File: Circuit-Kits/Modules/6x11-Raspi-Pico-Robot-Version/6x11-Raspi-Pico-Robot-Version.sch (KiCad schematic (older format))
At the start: 9 parts, among them J1 PWM, J2 PWM, J3 PWM, J4 PWM, J5 ANALOG, J6 ANALOG, J7 ANALOG, U1 ARDUINO-SERVO-PWM, U2 Pico

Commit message: Updated PCB with new footprint and pinout
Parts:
- removed U1: ARDUINO-SERVO-PWM, Crazy_Circuits:5x11-SERVO-ANALOG, symbol 5x11-Raspi-Pico-Robot-Version-rescue:ARDUINO-SERVO-PWM
- added U1: 6x11-PICO, Crazy_Circuits:6x11-PICO-ROBOT, symbol crazy_circuits:6x11-PICO
- J1, J2, J3, J4, J5, J6, J7: symbol 5x11-Raspi-Pico-Robot-Version-rescue:HEADER-MALE-3POS-TH-1x03-P0.1IN-crazy_circuits -> 6x11-Raspi-Pico-Robot-Version-rescue:HEADER-MALE-3POS-TH-1x03-P0.1IN-crazy_circuits-5x11-Raspi-Pico-Robot-Version-rescue
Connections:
- wire segments 74 -> 75
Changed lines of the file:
@@
 $EndDescr
 $Comp
-L 5x11-Raspi-Pico-Robot-Version-rescue:GND-crazy_circuits #PWR01
+L 6x11-Raspi-Pico-Robot-Version-rescue:GND-crazy_circuits-5x11-Raspi-Pico-Robot-Version-rescue #PWR01
 U 1 1 58FE4F4A
 P 3725 4225
@@
 A5
 $Comp
-L 5x11-Raspi-Pico-Robot-Version-rescue:HEADER-MALE-3POS-TH-1x03-P0.1IN-crazy_circuits J1
+L 6x11-Raspi-Pico-Robot-Version-rescue:HEADER-MALE-3POS-TH-1x03-P0.1IN-crazy_circuits-5x11-Raspi-Pico-Robot-Version-rescue J1
 U 1 1 58FE51EC
 P 3350 1675
@@
 $EndComp
 $Comp
-L 5x11-Raspi-Pico-Robot-Version-rescue:HEADER-MALE-3POS-TH-1x03-P0.1IN-crazy_circuits J5
+L 6x11-Raspi-Pico-Robot-Version-rescue:HEADER-MALE-3POS-TH-1x03-P0.1IN-crazy_circuits-5x11-Raspi-Pico-Robot-Version-rescue J5
 U 1 1 58FE54AA
 P 3350 3575
@@
 $EndComp
 $Comp
-L 5x11-Raspi-Pico-Robot-Version-rescue:HEADER-MALE-3POS-TH-1x03-P0.1IN-crazy_circuits J6
+L 6x11-Raspi-Pico-Robot-Version-rescue:HEADER-MALE-3POS-TH-1x03-P0.1IN-crazy_circuits-5x11-Raspi-Pico-Robot-Version-rescue J6
 U 1 1 58FE54F2
 P 3350 4050
@@
 $EndComp
 $Comp
-L 5x11-Raspi-Pico-Robot-Version-rescue:GND-crazy_circuits #PWR03
+L 6x11-Raspi-Pico-Robot-Version-rescue:GND-crazy_circuits-5x11-Raspi-Pico-Robot-Version-rescue #PWR03
 U 1 1 58FE5E9A
 P 5325 4275
@@
 Connection ~ 3725 3200
 $Comp
-L 5x11-Raspi-Pico-Robot-Version-rescue:HEADER-MALE-3POS-TH-1x03-P0.1IN-crazy_circuits J2
+L 6x11-Raspi-Pico-Robot-Version-rescue:HEADER-MALE-3POS-TH-1x03-P0.1IN-crazy_circuits-5x11-Raspi-Pico-Robot-Version-rescue J2
 U 1 1 5AF1C185
 P 3350 2150
@@
 $EndComp
 $Comp
-L 5x11-Raspi-Pico-Robot-Version-rescue:HEADER-MALE-3POS-TH-1x03-P0.1IN-crazy_circuits J3
+L 6x11-Raspi-Pico-Robot-Version-rescue:HEADER-MALE-3POS-TH-1x03-P0.1IN-crazy_circuits-5x11-Raspi-Pico-Robot-Version-rescue J3
 U 1 1 5AF1C1CE
 P 3350 2625
@@
 $EndComp
 $Comp
-L 5x11-Raspi-Pico-Robot-Version-rescue:HEADER-MALE-3POS-TH-1x03-P0.1IN-crazy_circuits J4
+L 6x11-Raspi-Pico-Robot-Version-rescue:HEADER-MALE-3POS-TH-1x03-P0.1IN-crazy_circuits-5x11-Raspi-Pico-Robot-Version-rescue J4
 U 1 1 5AF1C230
 P 3350 3100
@@
 $EndComp
 $Comp
-L 5x11-Raspi-Pico-Robot-Version-rescue:GND-crazy_circuits #PWR0102
+L 6x11-Raspi-Pico-Robot-Version-rescue:GND-crazy_circuits-5x11-Raspi-Pico-Robot-Version-rescue #PWR0102
 U 1 1 608B12B6
 P 9100 1850
@@
 	9100 1850 8825 1850
 $Comp
-L 5x11-Raspi-Pico-Robot-Version-rescue:GND-crazy_circuits #PWR0103
+L 6x11-Raspi-Pico-Robot-Version-rescue:GND-crazy_circuits-5x11-Raspi-Pico-Robot-Version-rescue #PWR0103
 U 1 1 608BAEE6
 P 9100 2350
@@
 	9100 2350 8825 2350
 $Comp
-L 5x11-Raspi-Pico-Robot-Version-rescue:GND-crazy_circuits #PWR0104
+L 6x11-Raspi-Pico-Robot-Version-rescue:GND-crazy_circuits-5x11-Raspi-Pico-Robot-Version-rescue #PWR0104
 U 1 1 608BCF87
 P 9100 2850
@@
 	9100 2850 8825 2850
 $Comp
-L 5x11-Raspi-Pico-Robot-Version-rescue:GND-crazy_circuits #PWR0105
+L 6x11-Raspi-Pico-Robot-Version-rescue:GND-crazy_circuits-5x11-Raspi-Pico-Robot-Version-rescue #PWR0105
 U 1 1 608BEE78
 P 9100 3350
@@
 	9100 3350 8825 3350
 $Comp
-L 5x11-Raspi-Pico-Robot-Version-rescue:GND-crazy_circuits #PWR0106
+L 6x11-Raspi-Pico-Robot-Version-rescue:GND-crazy_circuits-5x11-Raspi-Pico-Robot-Version-rescue #PWR0106
 U 1 1 608C380D
 P 7150 1850
@@
 	7150 1850 7425 1850
 $Comp
-L 5x11-Raspi-Pico-Robot-Version-rescue:GND-crazy_circuits #PWR0107
+L 6x11-Raspi-Pico-Robot-Version-rescue:GND-crazy_circuits-5x11-Raspi-Pico-Robot-Version-rescue #PWR0107
 U 1 1 608C5761
 P 7150 2350
@@
 	7150 2350 7425 2350
 $Comp
-L 5x11-Raspi-Pico-Robot-Version-rescue:GND-crazy_circuits #PWR0108
+L 6x11-Raspi-Pico-Robot-Version-rescue:GND-crazy_circuits-5x11-Raspi-Pico-Robot-Version-rescue #PWR0108
 U 1 1 608C7766
 P 7150 2850
@@
 	7150 2850 7425 2850
 $Comp
-L 5x11-Raspi-Pico-Robot-Version-rescue:GND-crazy_circuits #PWR0109
+L 6x11-Raspi-Pico-Robot-Version-rescue:GND-crazy_circuits-5x11-Raspi-Pico-Robot-Version-rescue #PWR0109
 U 1 1 608C98C7
 P 7150 3350
@@
 Wire Wire Line
 	7150 3350 7425 3350
-$Comp
-L crazy_circuits:3.3V #PWR0110
-U 1 1 608CB6CC
-P 5475 1200
-F 0 "#PWR0110" H 5475 1050 50  0001 C CNN
-F 1 "3.3V" V 5493 1328 50  0000 L CNN
-F 2 "" H 5475 1200 50  0000 C CNN
-F 3 "" H 5475 1200 50  0000 C CNN
-	1    5475 1200
-	0    -1   -1   0
-$EndComp
 $Comp
 L crazy_circuits:3.3V #PWR0111
@@
 Text GLabel 5475 2500 0    50   Input ~ 0
 IO8
-Text GLabel 5475 2600 0    50   Input ~ 0
-IO9
 Text GLabel 5475 2700 0    50   Input ~ 0
 IO10
@@
 	5475 2300 5700 2300
 $Comp
-L 5x11-Raspi-Pico-Robot-Version-rescue:HEADER-MALE-3POS-TH-1x03-P0.1IN-crazy_circuits J7
+L 6x11-Raspi-Pico-Robot-Version-rescue:HEADER-MALE-3POS-TH-1x03-P0.1IN-crazy_circuits-5x11-Raspi-Pico-Robot-Version-rescue J7
 U 1 1 608A960B
 P 3350 4675
@@
 $EndComp
 $Comp
-L 5x11-Raspi-Pico-Robot-Version-rescue:GND-crazy_circuits #PWR0117
+L 6x11-Raspi-Pico-Robot-Version-rescue:GND-crazy_circuits-5x11-Raspi-Pico-Robot-Version-rescue #PWR0117
 U 1 1 608A9E31
 P 3725 4875
@@
 	4325 3650 4325 4575
 $Comp
-L 5x11-Raspi-Pico-Robot-Version-rescue:GND-crazy_circuits #PWR0119
+L 6x11-Raspi-Pico-Robot-Version-rescue:GND-crazy_circuits-5x11-Raspi-Pico-Robot-Version-rescue #PWR0119
 U 1 1 608B6490
 P 5575 1100
@@
 Wire Wire Line
 	3550 4575 4325 4575
-$Comp
-L 5x11-Raspi-Pico-Robot-Version-rescue:ARDUINO-SERVO-PWM U1
-U 1 1 608DB815
-P 6000 2750
-F 0 "U1" H 5822 2971 50  0000 R CNN
-F 1 "ARDUINO-SERVO-PWM" H 5822 2880 50  0000 R CNN
-F 2 "Crazy_Circuits:5x11-SERVO-ANALOG" H 6000 2750 50  0001 C CNN
-F 3 "" H 6000 2750 50  0001 C CNN
-	1    6000 2750
-	-1   0    0    -1
-$EndComp
 Text GLabel 8825 2150 2    50   Input ~ 0
 AREF
 Text GLabel 5700 1300 0    50   Input ~ 0
 AREF
+$Comp
+L crazy_circuits:6x11-PICO U1
+U 1 1 60AB76E0
+P 5950 2900
+F 0 "U1" H 5722 3271 50  0000 R CNN
+F 1 "6x11-PICO" H 5722 3180 50  0000 R CNN
+F 2 "Crazy_Circuits:6x11-PICO-ROBOT" H 5950 2900 50  0001 C CNN
+F 3 "" H 5950 2900 50  0001 C CNN
+	1    5950 2900
+	-1   0    0    -1
+$EndComp
+$Comp
+L crazy_circuits:3.3V #PWR0110
+U 1 1 608CB6CC
+P 5475 1200
+F 0 "#PWR0110" H 5475 1050 50  0001 C CNN
+F 1 "3.3V" V 5493 1328 50  0000 L CNN
+F 2 "" H 5475 1200 50  0000 C CNN
+F 3 "" H 5475 1200 50  0000 C CNN
+	1    5475 1200
+	0    -1   -1   0
+$EndComp
+Text GLabel 5475 2600 0    50   Input ~ 0
+IO9
+Wire Wire Line
+	5475 2600 5700 2600
 $EndSCHEMATC

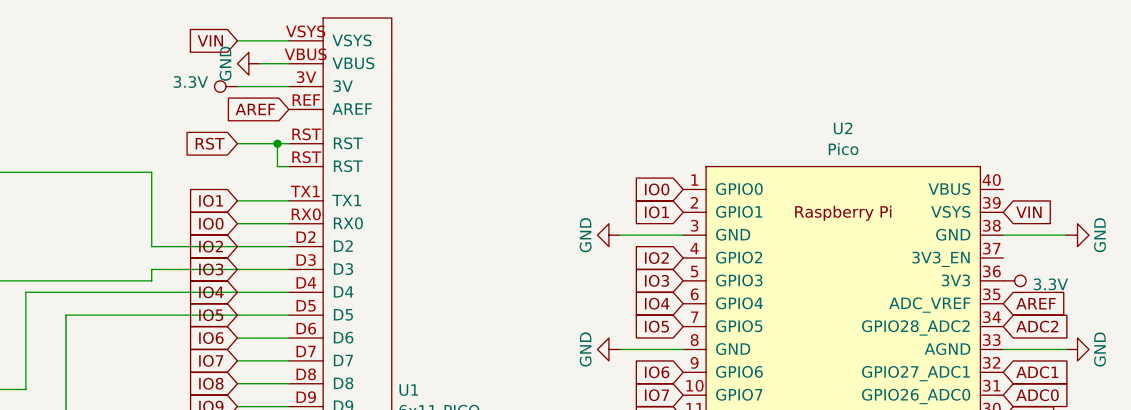
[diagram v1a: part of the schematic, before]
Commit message: Design Changes
* Removed D0 and D16
* Shifted pins
* Added silkscreen labels for 3v
* Broke out VBUS and VSYS
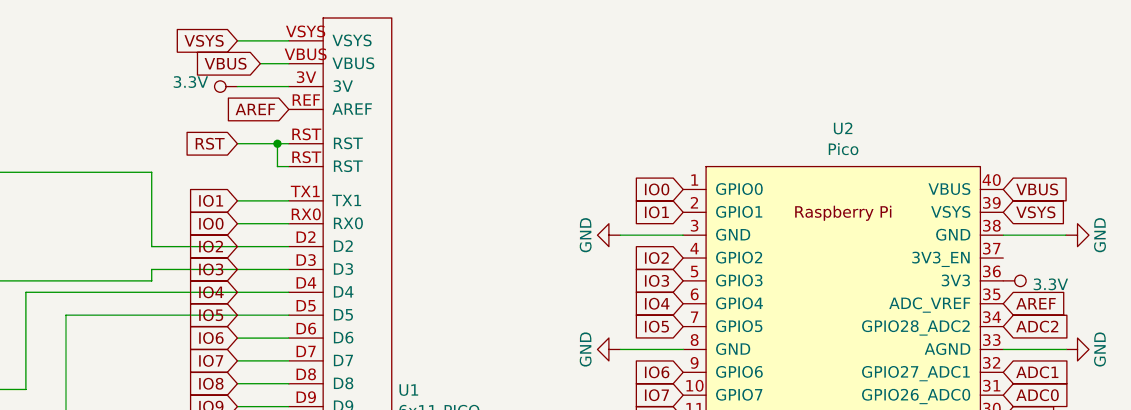
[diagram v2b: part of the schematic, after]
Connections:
- net GND: no longer U1.VBUS
- net VBUS: now reaches U2.40 (VBUS)
- net VBUS: now also U1.VBUS
- net VIN renamed VSYS
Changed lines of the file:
@@
 Text GLabel 8825 2650 2    50   Input ~ 0
 RST
-Text GLabel 5475 1000 0    50   Input ~ 0
-VIN
 Text Notes 2250 3650 0    50   ~ 0
 Pico is not 5v Tolerant.
 Text GLabel 8825 1750 2    50   Input ~ 0
-VIN
+VSYS
 $Comp
 L crazy_circuits:3.3V #PWR0101
@@
 Wire Wire Line
 	4325 3650 4325 4575
-$Comp
-L 6x11-Raspi-Pico-Robot-Version-rescue:GND-crazy_circuits-5x11-Raspi-Pico-Robot-Version-rescue #PWR0119
-U 1 1 608B6490
-P 5575 1100
-F 0 "#PWR0119" H 5575 850 50  0001 C CNN
-F 1 "GND" H 5575 950 50  0000 C CNN
-F 2 "" H 5575 1100 50  0000 C CNN
-F 3 "" H 5575 1100 50  0000 C CNN
-	1    5575 1100
-	0    1    1    0
-$EndComp
 Wire Wire Line
 	5700 1100 5575 1100
@@
 Wire Wire Line
 	5475 2600 5700 2600
+Text GLabel 8825 1650 2    50   Input ~ 0
+VBUS
+Text GLabel 5575 1100 0    50   Input ~ 0
+VBUS
+Text GLabel 5475 1000 0    50   Input ~ 0
+VSYS
 $EndSCHEMATC

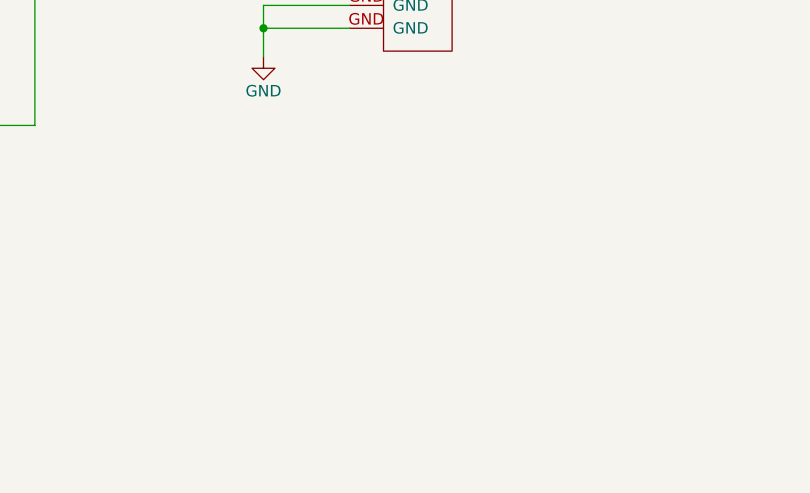
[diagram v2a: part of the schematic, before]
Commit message: Added Power LED and Resistor to schematic
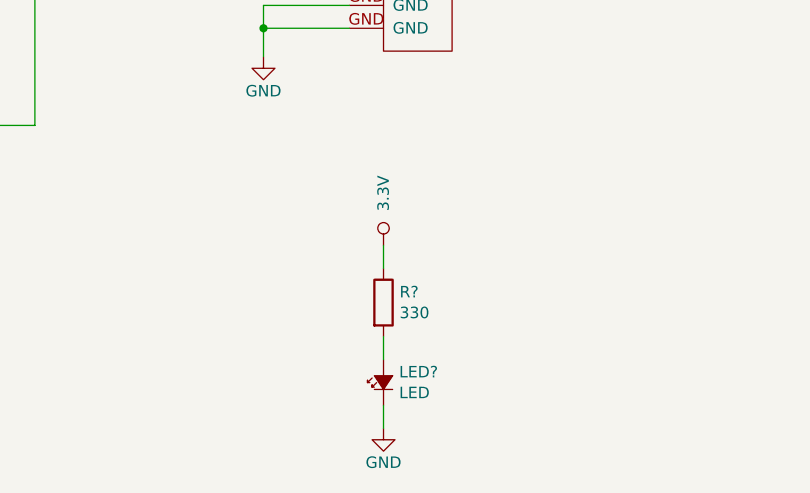
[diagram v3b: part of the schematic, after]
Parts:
- added LED?: LED, LED, symbol crazy_circuits:LED
- added R?: 330, symbol Device:R
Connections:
- net 3.3V: now also R?.1
- net GND: now also LED?.-
- new net: LED?.+, R?.2
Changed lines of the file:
@@
 Text GLabel 5475 1000 0    50   Input ~ 0
 VSYS
+$Comp
+L crazy_circuits:LED LED?
+U 1 1 625CD2FF
+P 5850 5700
+F 0 "LED?" H 5918 5746 50  0000 L CNN
+F 1 "LED" H 5918 5655 50  0000 L CNN
+F 2 "LED" H 5850 5500 50  0001 C CIN
+F 3 "http://www.marktechopto.com/products/datasheet/MT2118-G-A" V 5850 5700 5   0001 C CNN
+	1    5850 5700
+	1    0    0    -1
+$EndComp
+$Comp
+L Device:R R?
+U 1 1 625CE12D
+P 5850 5350
+F 0 "R?" H 5920 5396 50  0000 L CNN
+F 1 "330" H 5920 5305 50  0000 L CNN
+F 2 "" V 5780 5350 50  0001 C CNN
+F 3 "~" H 5850 5350 50  0001 C CNN
+	1    5850 5350
+	1    0    0    -1
+$EndComp
+$Comp
+L crazy_circuits:3.3V #PWR?
+U 1 1 625CE73B
+P 5850 5100
+F 0 "#PWR?" H 5850 4950 50  0001 C CNN
+F 1 "3.3V" V 5850 5250 50  0000 L CNN
+F 2 "" H 5850 5100 50  0000 C CNN
+F 3 "" H 5850 5100 50  0000 C CNN
+	1    5850 5100
+	1    0    0    -1
+$EndComp
+Wire Wire Line
+	5850 5100 5850 5200
+Wire Wire Line
+	5850 5500 5850 5600
+$Comp
+L 6x11-Raspi-Pico-Robot-Version-rescue:GND-crazy_circuits-5x11-Raspi-Pico-Robot-Version-rescue #PWR?
+U 1 1 625D32FF
+P 5850 5900
+F 0 "#PWR?" H 5850 5650 50  0001 C CNN
+F 1 "GND" H 5850 5750 50  0000 C CNN
+F 2 "" H 5850 5900 50  0000 C CNN
+F 3 "" H 5850 5900 50  0000 C CNN
+	1    5850 5900
+	1    0    0    -1
+$EndComp
+Wire Wire Line
+	5850 5800 5850 5900
 $EndSCHEMATC

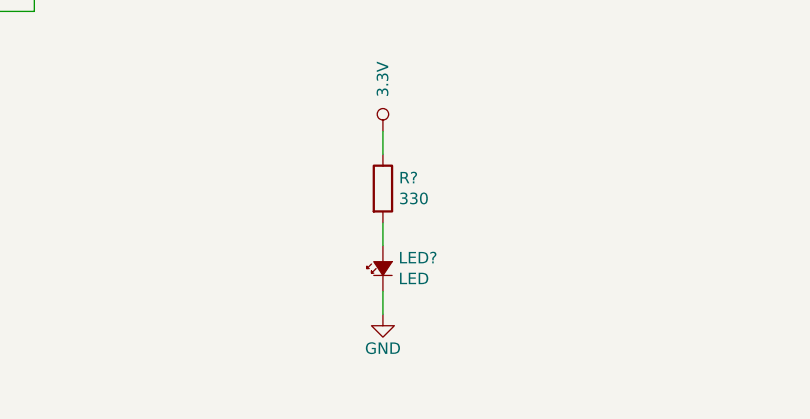
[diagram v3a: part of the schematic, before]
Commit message: Change LED Schematic Symbol
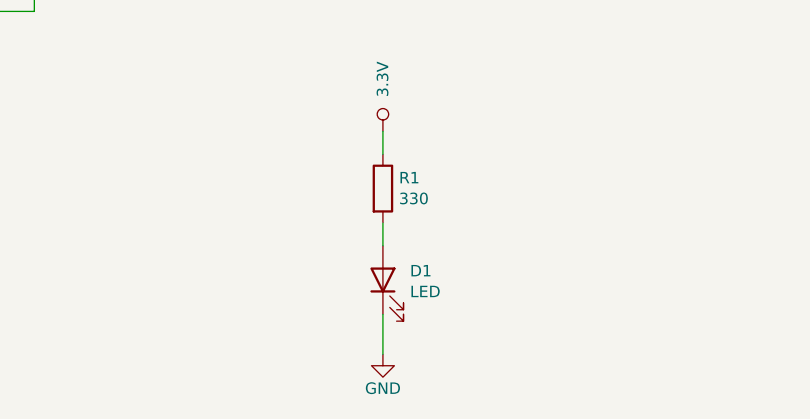
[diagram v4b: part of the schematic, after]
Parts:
- removed LED?: LED, LED, symbol crazy_circuits:LED
- added D1: LED, LED_SMD:LED_0603_1608Metric, symbol Device:LED
- R1: renamed from R?; footprint (none) -> Resistor_SMD:R_0603_1608Metric
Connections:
- net GND: now also D1.1 (K)
- net at R1.2: now also D1.2 (A)
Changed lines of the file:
@@
 VSYS
 $Comp
-L crazy_circuits:LED LED?
-U 1 1 625CD2FF
-P 5850 5700
-F 0 "LED?" H 5918 5746 50  0000 L CNN
-F 1 "LED" H 5918 5655 50  0000 L CNN
-F 2 "LED" H 5850 5500 50  0001 C CIN
-F 3 "http://www.marktechopto.com/products/datasheet/MT2118-G-A" V 5850 5700 5   0001 C CNN
-	1    5850 5700
-	1    0    0    -1
-$EndComp
-$Comp
-L Device:R R?
+L Device:R R1
 U 1 1 625CE12D
 P 5850 5350
-F 0 "R?" H 5920 5396 50  0000 L CNN
+F 0 "R1" H 5920 5396 50  0000 L CNN
 F 1 "330" H 5920 5305 50  0000 L CNN
-F 2 "" V 5780 5350 50  0001 C CNN
+F 2 "Resistor_SMD:R_0603_1608Metric" V 5780 5350 50  0001 C CNN
 F 3 "~" H 5850 5350 50  0001 C CNN
 	1    5850 5350
@@
 $EndComp
 $Comp
-L crazy_circuits:3.3V #PWR?
+L crazy_circuits:3.3V #PWR0119
 U 1 1 625CE73B
 P 5850 5100
-F 0 "#PWR?" H 5850 4950 50  0001 C CNN
+F 0 "#PWR0119" H 5850 4950 50  0001 C CNN
 F 1 "3.3V" V 5850 5250 50  0000 L CNN
 F 2 "" H 5850 5100 50  0000 C CNN
@@
 	5850 5500 5850 5600
 $Comp
-L 6x11-Raspi-Pico-Robot-Version-rescue:GND-crazy_circuits-5x11-Raspi-Pico-Robot-Version-rescue #PWR?
+L 6x11-Raspi-Pico-Robot-Version-rescue:GND-crazy_circuits-5x11-Raspi-Pico-Robot-Version-rescue #PWR0120
 U 1 1 625D32FF
-P 5850 5900
-F 0 "#PWR?" H 5850 5650 50  0001 C CNN
-F 1 "GND" H 5850 5750 50  0000 C CNN
-F 2 "" H 5850 5900 50  0000 C CNN
-F 3 "" H 5850 5900 50  0000 C CNN
-	1    5850 5900
+P 5850 6075
+F 0 "#PWR0120" H 5850 5825 50  0001 C CNN
+F 1 "GND" H 5850 5925 50  0000 C CNN
+F 2 "" H 5850 6075 50  0000 C CNN
+F 3 "" H 5850 6075 50  0000 C CNN
+	1    5850 6075
 	1    0    0    -1
 $EndComp
+$Comp
+L Device:LED D1
+U 1 1 625DF38F
+P 5850 5750
+F 0 "D1" V 5889 5632 50  0000 R CNN
+F 1 "LED" V 5798 5632 50  0000 R CNN
+F 2 "LED_SMD:LED_0603_1608Metric" H 5850 5750 50  0001 C CNN
+F 3 "~" H 5850 5750 50  0001 C CNN
+	1    5850 5750
+	0    -1   -1   0
+$EndComp
 Wire Wire Line
-	5850 5800 5850 5900
+	5850 5900 5850 6075
 $EndSCHEMATC

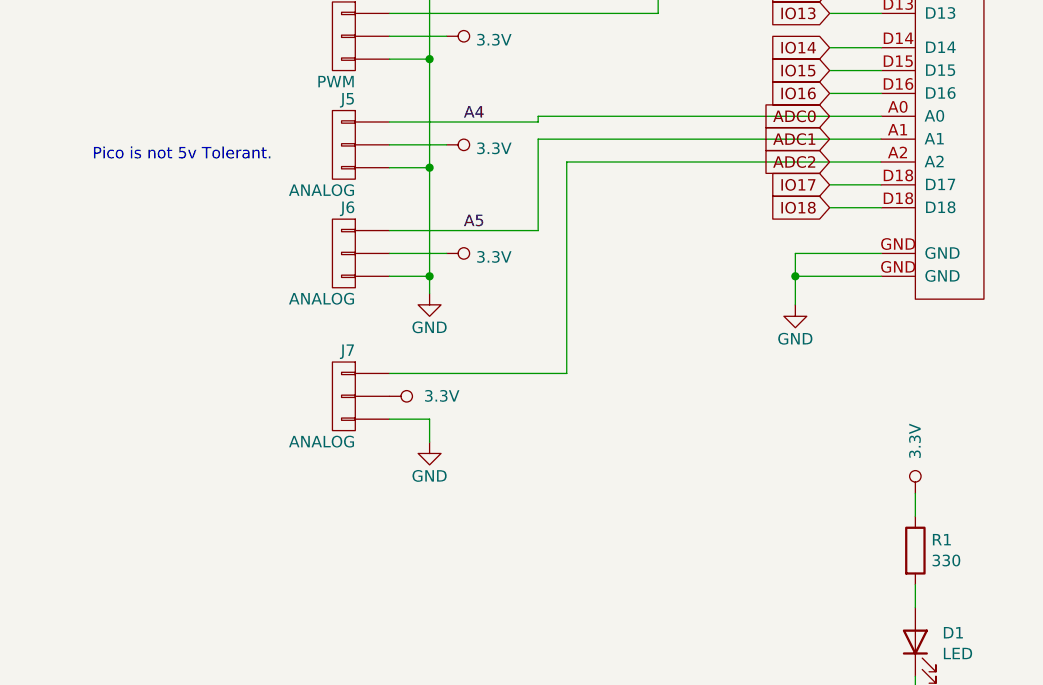
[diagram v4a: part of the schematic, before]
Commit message: Added new Vsys Connector, replaced old a2 connector.
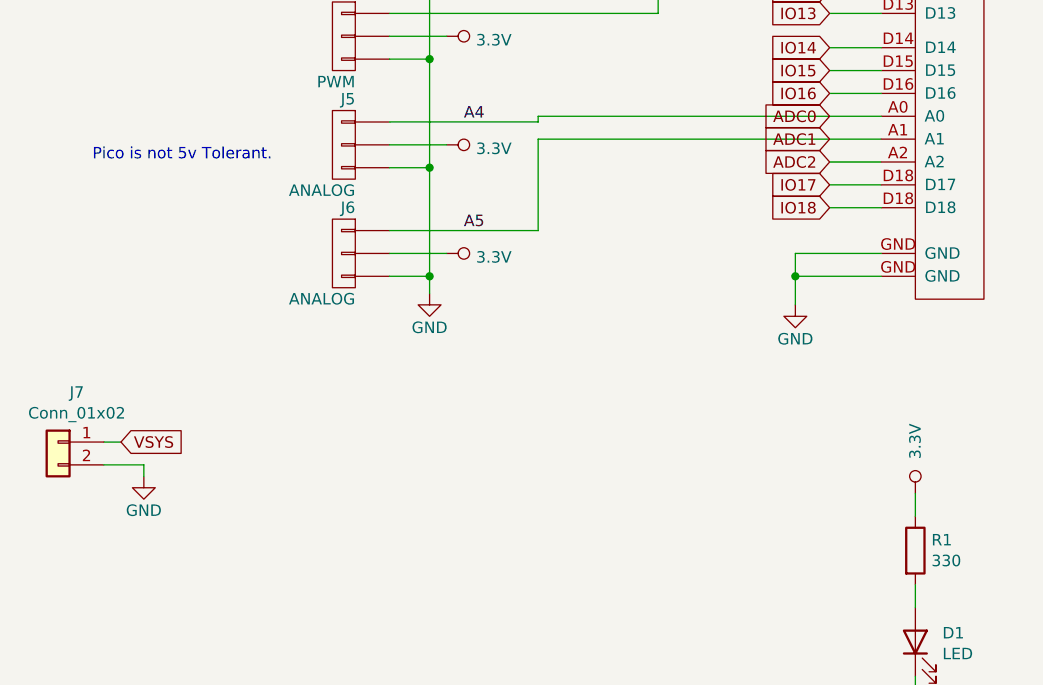
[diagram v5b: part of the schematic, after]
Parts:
- removed J7: ANALOG, Crazy_NonLego:CONN-HEADER-STRAIGHT-P2.54MM-1x03, symbol 6x11-Raspi-Pico-Robot-Version-rescue:HEADER-MALE-3POS-TH-1x03-P0.1IN-crazy_circ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
- added J7: Conn_01x02, Crazy_NonLego:CONN-HEADER-STRAIGHT-P2.54MM-1x02, symbol Connector_Generic:Conn_01x02
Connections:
- net GND: now also J7.2 (Pin_2)
- net VSYS: now also J7.1 (Pin_1)
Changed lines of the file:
@@
 	5475 2300 5700 2300
-$Comp
-L 6x11-Raspi-Pico-Robot-Version-rescue:HEADER-MALE-3POS-TH-1x03-P0.1IN-crazy_circuits-5x11-Raspi-Pico-Robot-Version-rescue J7
-U 1 1 608A960B
-P 3350 4675
-F 0 "J7" H 3300 4875 50  0000 L CNN
-F 1 "ANALOG" H 3300 4475 50  0000 L CNN
-F 2 "Crazy_NonLego:CONN-HEADER-STRAIGHT-P2.54MM-1x03" H 3350 4325 50  0001 C CIN
-F 3 "https://cdn.harwin.com/pdfs/60page140.pdf" H 3350 4675 5   0001 C CNN
-F 4 "HEADER MALE 3POS TH 1x03 0.1IN" H 3350 4325 50  0001 C CIN "Description"
-F 5 "Harwin" H 3350 4325 50  0001 C CIN "MF_Name"
-F 6 "M20-9990346" H 3350 4325 50  0001 C CIN "MF_PN"
-F 7 "Digikey" H 3350 4325 50  0001 C CIN "S1_Name"
-F 8 "952-2264-ND" H 3350 4325 50  0001 C CIN "S1_PN"
-F 9 "th" H 3350 4675 50  0001 C CNN "Type"
-	1    3350 4675
-	-1   0    0    -1
-$EndComp
 $Comp
 L 6x11-Raspi-Pico-Robot-Version-rescue:GND-crazy_circuits-5x11-Raspi-Pico-Robot-Version-rescue #PWR0117
 U 1 1 608A9E31
-P 3725 4875
-F 0 "#PWR0117" H 3725 4625 50  0001 C CNN
-F 1 "GND" H 3725 4725 50  0000 C CNN
-F 2 "" H 3725 4875 50  0000 C CNN
-F 3 "" H 3725 4875 50  0000 C CNN
-	1    3725 4875
+P 2475 5025
+F 0 "#PWR0117" H 2475 4775 50  0001 C CNN
+F 1 "GND" H 2475 4875 50  0000 C CNN
+F 2 "" H 2475 5025 50  0000 C CNN
+F 3 "" H 2475 5025 50  0000 C CNN
+	1    2475 5025
 	1    0    0    -1
-$EndComp
-Wire Wire Line
-	3550 4775 3725 4775
-Wire Wire Line
-	3725 4775 3725 4875
-$Comp
-L crazy_circuits:3.3V #PWR0118
-U 1 1 608ABE47
-P 3550 4675
-F 0 "#PWR0118" H 3550 4525 50  0001 C CNN
-F 1 "3.3V" V 3550 4825 50  0000 L CNN
-F 2 "" H 3550 4675 50  0000 C CNN
-F 3 "" H 3550 4675 50  0000 C CNN
-	1    3550 4675
-	0    1    1    0
 $EndComp
 Wire Wire Line
@@
 	4200 3550 4200 3950
 Wire Wire Line
-	5700 3650 4325 3650
-Wire Wire Line
-	4325 3650 4325 4575
-Wire Wire Line
 	5700 1100 5575 1100
-Wire Wire Line
-	3550 4575 4325 4575
 Text GLabel 8825 2150 2    50   Input ~ 0
 AREF
@@
 Wire Wire Line
 	5850 5900 5850 6075
+$Comp
+L Connector_Generic:Conn_01x02 J7
+U 1 1 625EAD5E
+P 2100 4875
+F 0 "J7" H 2018 5092 50  0000 C CNN
+F 1 "Conn_01x02" H 2018 5001 50  0000 C CNN
+F 2 "Crazy_NonLego:CONN-HEADER-STRAIGHT-P2.54MM-1x02" H 2100 4875 50  0001 C CNN
+F 3 "~" H 2100 4875 50  0001 C CNN
+	1    2100 4875
+	-1   0    0    -1
+$EndComp
+Text GLabel 2375 4875 2    50   Input ~ 0
+VSYS
+Wire Wire Line
+	5475 3650 5700 3650
+Wire Wire Line
+	2375 4875 2300 4875
+Wire Wire Line
+	2300 4975 2475 4975
+Wire Wire Line
+	2475 4975 2475 5025
 $EndSCHEMATC
